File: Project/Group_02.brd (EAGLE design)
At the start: 71.1 x 44.5 mm, 29 parts, among them J1 POWER_JACKPTH_LOCK, U1 +12v

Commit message: Posizionamento holes
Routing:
- net GND: track 10.4 -> 16.1 mm
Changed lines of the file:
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@@
 <setting verticaltext="up"/>
 </settings>
-<grid distance="0.05" unitdist="inch" unit="mm" style="lines" multiple="1" display="yes" altdistance="0.005" altunitdist="inch" altunit="mm"/>
+<grid distance="0.05" unitdist="inch" unit="mil" style="lines" multiple="1" display="yes" altdistance="0.005" altunitdist="inch" altunit="mm"/>
 <layers>
 <layer number="1" name="Top" color="4" fill="1" visible="yes" active="yes"/>
@@
 <dimension x1="-1.27" y1="0" x2="-1.27" y2="44.45" x3="-2.54" y3="22.225" textsize="1.778" layer="51"/>
 <dimension x1="0" y1="46.99" x2="71.12" y2="46.99" x3="35.56" y3="45.72" textsize="1.778" layer="51"/>
+<hole x="3.175" y="42.291" drill="0.9"/>
+<hole x="3.175" y="2.032" drill="0.9"/>
+<hole x="68.58" y="2.032" drill="0.9"/>
+<hole x="68.58" y="42.291" drill="0.9"/>
 </plain>
 <attributes>
@@
 </class>
 </classes>
-<designrules name="default">
+<designrules name="Group_02">
 <description language="de">&lt;b&gt;EAGLE Design Rules&lt;/b&gt;
 &lt;p&gt;
@@
 <param name="mdViaViaSameLayer" value="6mil"/>
 <param name="mnLayersViaInSmd" value="2"/>
-<param name="mdCopperDimension" value="40mil"/>
-<param name="mdDrill" value="6mil"/>
+<param name="mdCopperDimension" value="8mil"/>
+<param name="mdDrill" value="18mil"/>
 <param name="mdSmdStop" value="0mil"/>
-<param name="msWidth" value="6mil"/>
-<param name="msDrill" value="0.35mm"/>
+<param name="msWidth" value="10mil"/>
+<param name="msDrill" value="8mil"/>
 <param name="msMicroVia" value="9.99mm"/>
 <param name="msBlindViaRatio" value="0.5"/>
@@
 <param name="rvMicroViaOuter" value="0.25"/>
 <param name="rvMicroViaInner" value="0.25"/>
-<param name="rlMinPadTop" value="10mil"/>
+<param name="rlMinPadTop" value="8mil"/>
 <param name="rlMaxPadTop" value="20mil"/>
-<param name="rlMinPadInner" value="10mil"/>
+<param name="rlMinPadInner" value="6mil"/>
 <param name="rlMaxPadInner" value="20mil"/>
-<param name="rlMinPadBottom" value="10mil"/>
+<param name="rlMinPadBottom" value="8mil"/>
 <param name="rlMaxPadBottom" value="20mil"/>
-<param name="rlMinViaOuter" value="8mil"/>
+<param name="rlMinViaOuter" value="6mil"/>
 <param name="rlMaxViaOuter" value="20mil"/>
-<param name="rlMinViaInner" value="8mil"/>
+<param name="rlMinViaInner" value="6mil"/>
 <param name="rlMaxViaInner" value="20mil"/>
 <param name="rlMinMicroViaOuter" value="4mil"/>
@@
 <param name="mvStopFrame" value="1"/>
 <param name="mvCreamFrame" value="0"/>
-<param name="mlMinStopFrame" value="4mil"/>
-<param name="mlMaxStopFrame" value="4mil"/>
+<param name="mlMinStopFrame" value="8mil"/>
+<param name="mlMaxStopFrame" value="8mil"/>
 <param name="mlMinCreamFrame" value="0mil"/>
 <param name="mlMaxCreamFrame" value="0mil"/>
@@
 <wire x1="49.149" y1="31.281" x2="50.4834" y2="29.9466" width="0.1524" layer="1"/>
 <wire x1="50.4834" y1="29.9466" x2="52.04596875" y2="29.9466" width="0.1524" layer="1"/>
-<wire x1="20.104" y1="36.395" x2="20.32" y2="36.395" width="0.1524" layer="1"/>
 <via x="21.9506" y="36.9467375" extent="1-16" drill="0.35"/>
 <wire x1="18.704" y1="37.395" x2="18.704" y2="37.811" width="0.1524" layer="1"/>
@@
 <contactref element="U$2" pad="8"/>
 <contactref element="U$2" pad="3"/>
-<polygon width="0.2032" layer="1">
+<polygon width="0.2032" layer="1" isolate="0.3048">
 <vertex x="0" y="0"/>
 <vertex x="0" y="44.45"/>
@@
 <wire x1="34.13896875" y1="37.6936" x2="29.8704" y2="37.6936" width="0.1524" layer="16"/>
 <wire x1="29.8704" y1="37.6936" x2="28.702" y2="38.862" width="0.1524" layer="16"/>
+<wire x1="20.104" y1="36.795" x2="20.139" y2="36.83" width="0.1524" layer="1"/>
+<wire x1="20.139" y1="36.83" x2="21.3438" y2="36.83" width="0.1524" layer="1"/>
+<wire x1="21.3438" y1="36.83" x2="21.3438" y2="37.1980875" width="0.1524" layer="1"/>
+<wire x1="21.3438" y1="37.1980875" x2="21.69925" y2="37.5535375" width="0.1524" layer="1"/>
+<wire x1="21.69925" y1="37.5535375" x2="22.20195" y2="37.5535375" width="0.1524" layer="1"/>
+<wire x1="22.20195" y1="37.5535375" x2="22.5574" y2="37.1980875" width="0.1524" layer="1"/>
+<wire x1="22.5574" y1="37.1980875" x2="22.5574" y2="37.1326" width="0.1524" layer="1"/>
+<wire x1="22.987" y1="36.703" x2="24.892" y2="36.703" width="0.1524" layer="1"/>
+<wire x1="22.5574" y1="37.1326" x2="22.987" y2="36.703" width="0.1524" layer="1"/>
 </signal>
 <signal name="12V">
@@
 <contactref element="R8" pad="1"/>
 <wire x1="31.75" y1="31.75" x2="31.75" y2="33.44" width="0.2032" layer="1"/>
-<wire x1="31.75" y1="33.44" x2="33.02" y2="34.71" width="0.2032" layer="1"/>
+<wire x1="31.75" y1="33.44" x2="32.175" y2="33.865" width="0.2032" layer="1"/>
+<wire x1="32.175" y1="33.865" x2="33.02" y2="34.71" width="0.2032" layer="1"/>
 <wire x1="33.02" y1="34.71" x2="33.417965625" y2="34.312034375" width="0.2032" layer="1"/>
 <wire x1="33.417965625" y1="34.312034375" x2="34.267965625" y2="34.312034375" width="0.2032" layer="1"/>
@@
 <wire x1="13.86659375" y1="35.2298" x2="13.753196875" y2="35.343196875" width="0.2032" layer="1"/>
 <wire x1="13.753196875" y1="35.343196875" x2="13.626196875" y2="35.343196875" width="0.2032" layer="1"/>
-<wire x1="13.626196875" y1="35.343196875" x2="10.16" y2="31.877" width="0.2032" layer="1"/>
-<wire x1="16.075" y1="36.395" x2="14.9098" y2="35.2298" width="0.2032" layer="1"/>
+<wire x1="13.626196875" y1="35.343196875" x2="10.16" y2="31.877" width="0.254" layer="1"/>
+<wire x1="16.075" y1="36.395" x2="14.9098" y2="35.2298" width="0.254" layer="1"/>
 <wire x1="14.9098" y1="35.2298" x2="13.86659375" y2="35.2298" width="0.2032" layer="1"/>
 </signal>
@@
 <wire x1="12.7" y1="31.623" x2="12.7" y2="33.02" width="0.2032" layer="1"/>
 <wire x1="14.5542" y1="34.8742" x2="15.0571" y2="34.8742" width="0.2032" layer="1"/>
-<wire x1="16.1779" y1="35.995" x2="18.504" y2="35.995" width="0.2032" layer="1"/>
+<wire x1="16.1779" y1="35.995" x2="18.504" y2="35.995" width="0.254" layer="1"/>
 <wire x1="15.0571" y1="34.8742" x2="16.1779" y2="35.995" width="0.2032" layer="1"/>
 <wire x1="12.7" y1="33.02" x2="14.5542" y2="34.8742" width="0.2032" layer="1"/>

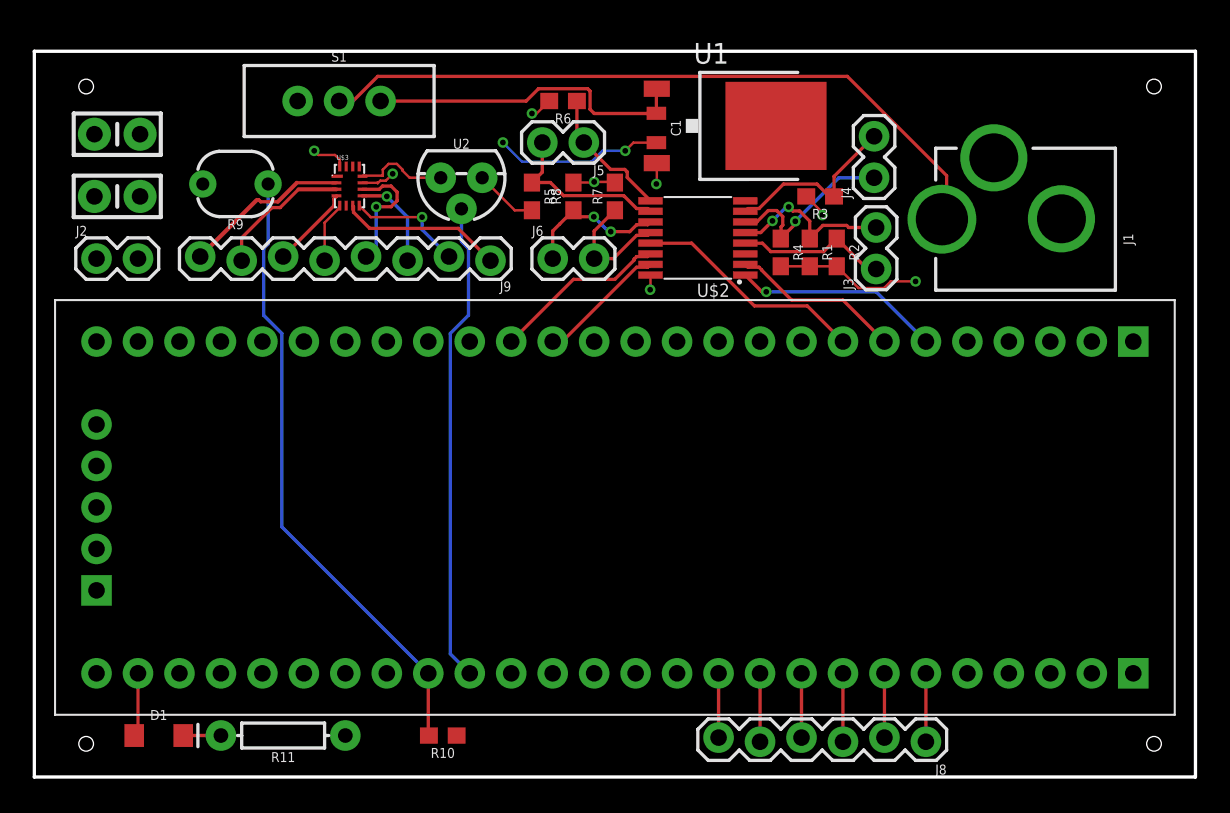
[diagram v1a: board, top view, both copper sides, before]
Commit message: Aggiornamento M3 holes
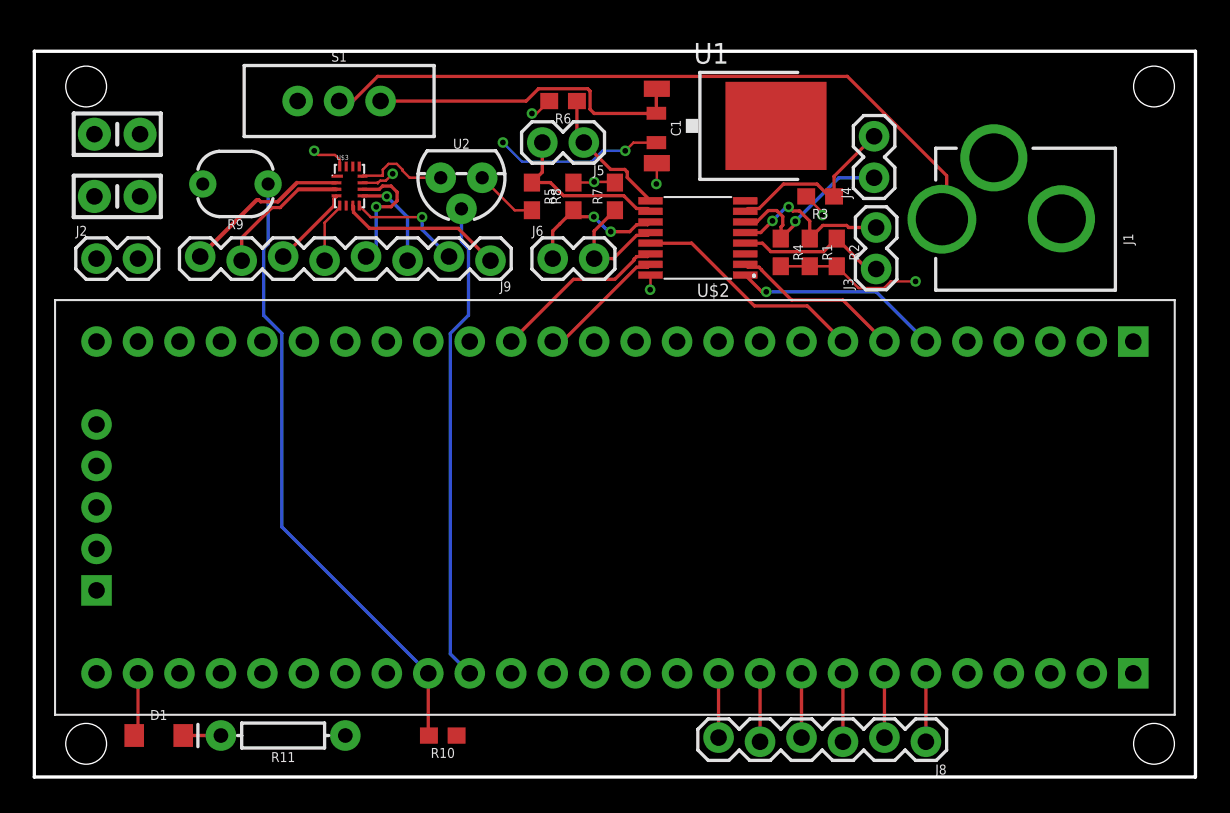
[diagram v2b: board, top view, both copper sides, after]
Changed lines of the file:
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@@
 <setting verticaltext="up"/>
 </settings>
-<grid distance="0.05" unitdist="inch" unit="mil" style="lines" multiple="1" display="yes" altdistance="0.005" altunitdist="inch" altunit="mm"/>
+<grid distance="0.05" unitdist="inch" unit="mm" style="lines" multiple="1" display="yes" altdistance="0.005" altunitdist="inch" altunit="mm"/>
 <layers>
 <layer number="1" name="Top" color="4" fill="1" visible="yes" active="yes"/>
@@
 <dimension x1="-1.27" y1="0" x2="-1.27" y2="44.45" x3="-2.54" y3="22.225" textsize="1.778" layer="51"/>
 <dimension x1="0" y1="46.99" x2="71.12" y2="46.99" x3="35.56" y3="45.72" textsize="1.778" layer="51"/>
-<hole x="3.175" y="42.291" drill="0.9"/>
-<hole x="3.175" y="2.032" drill="0.9"/>
-<hole x="68.58" y="2.032" drill="0.9"/>
-<hole x="68.58" y="42.291" drill="0.9"/>
+<hole x="3.175" y="42.291" drill="2.5"/>
+<hole x="3.175" y="2.032" drill="2.5"/>
+<hole x="68.58" y="2.032" drill="2.5"/>
+<hole x="68.58" y="42.291" drill="2.5"/>
 </plain>
 <attributes>
@@
 <via x="17.145" y="38.354" extent="1-16" drill="0.35"/>
 <wire x1="18.415" y1="38.1" x2="17.399" y2="38.1" width="0.1524" layer="1"/>
+<wire x1="47.498" y1="31.281" x2="48.26" y2="34.4172" width="0" layer="19" extent="1-1"/>
+<wire x1="37.74" y1="30.745" x2="45.72" y2="31.281" width="0" layer="19" extent="1-1"/>
+<wire x1="38.1" y1="36.322" x2="37.74" y2="30.745" width="0" layer="19" extent="1-1"/>
+<wire x1="35.56" y1="36.41" x2="38.1" y2="36.322" width="0" layer="19" extent="1-1"/>
+<wire x1="30.48" y1="34.71" x2="33.02" y2="36.41" width="0" layer="19" extent="1-1"/>
+<wire x1="30.48" y1="40.64" x2="33.02" y2="36.41" width="0" layer="19" extent="1-1"/>
+<wire x1="21.9506" y1="36.9467375" x2="27.432" y2="36.703" width="0" layer="19" extent="1-1"/>
+<wire x1="18.704" y1="37.395" x2="20.104" y2="36.395" width="0" layer="19" extent="1-1"/>
+<wire x1="10.319" y1="36.322" x2="17.145" y2="38.354" width="0" layer="19" extent="1-1"/>
+<wire x1="6.477" y1="35.56" x2="10.319" y2="36.322" width="0" layer="19" extent="1-1"/>
+<wire x1="6.477" y1="39.37" x2="6.477" y2="35.56" width="0" layer="19" extent="1-1"/>
+<wire x1="6.35" y1="31.75" x2="6.477" y2="35.56" width="0" layer="19" extent="1-1"/>
+<wire x1="3.81" y1="26.67" x2="6.35" y2="31.75" width="0" layer="19" extent="1-1"/>
+<wire x1="67.31" y1="6.35" x2="53.975" y2="30.353" width="0" layer="19" extent="1-1"/>
 </signal>
 <signal name="GND">
@@
 <wire x1="22.987" y1="36.703" x2="24.892" y2="36.703" width="0.1524" layer="1"/>
 <wire x1="22.5574" y1="37.1326" x2="22.987" y2="36.703" width="0.1524" layer="1"/>
+<wire x1="62.912" y1="34.1884" x2="58.769" y2="37.9246" width="0" layer="19" extent="1-1"/>
+<wire x1="45.426" y1="39.878" x2="58.769" y2="37.9246" width="0" layer="19" extent="1-1"/>
+<wire x1="43.54" y1="35.295" x2="45.426" y2="39.878" width="0" layer="19" extent="1-1"/>
+<wire x1="43.54" y1="32.045" x2="43.54" y2="35.295" width="0" layer="19" extent="1-1"/>
+<wire x1="38.1" y1="38.851" x2="43.54" y2="35.295" width="0" layer="19" extent="1-1"/>
+<wire x1="24.892" y1="36.703" x2="28.702" y2="38.862" width="0" layer="19" extent="1-1"/>
+<wire x1="3.683" y1="35.56" x2="20.104" y2="36.795" width="0" layer="19" extent="1-1"/>
+<wire x1="3.683" y1="39.37" x2="3.683" y2="35.56" width="0" layer="19" extent="1-1"/>
+<wire x1="3.81" y1="31.75" x2="3.683" y2="35.56" width="0" layer="19" extent="1-1"/>
+<wire x1="6.35" y1="26.67" x2="3.81" y2="31.75" width="0" layer="19" extent="1-1"/>
+<wire x1="19.05" y1="2.54" x2="6.35" y2="26.67" width="0" layer="19" extent="1-1"/>
+<wire x1="25.869" y1="2.54" x2="19.05" y2="2.54" width="0" layer="19" extent="1-1"/>
+<wire x1="64.77" y1="6.35" x2="62.912" y2="34.1884" width="0" layer="19" extent="1-1"/>
 </signal>
 <signal name="12V">

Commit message: Routing width 10 mils
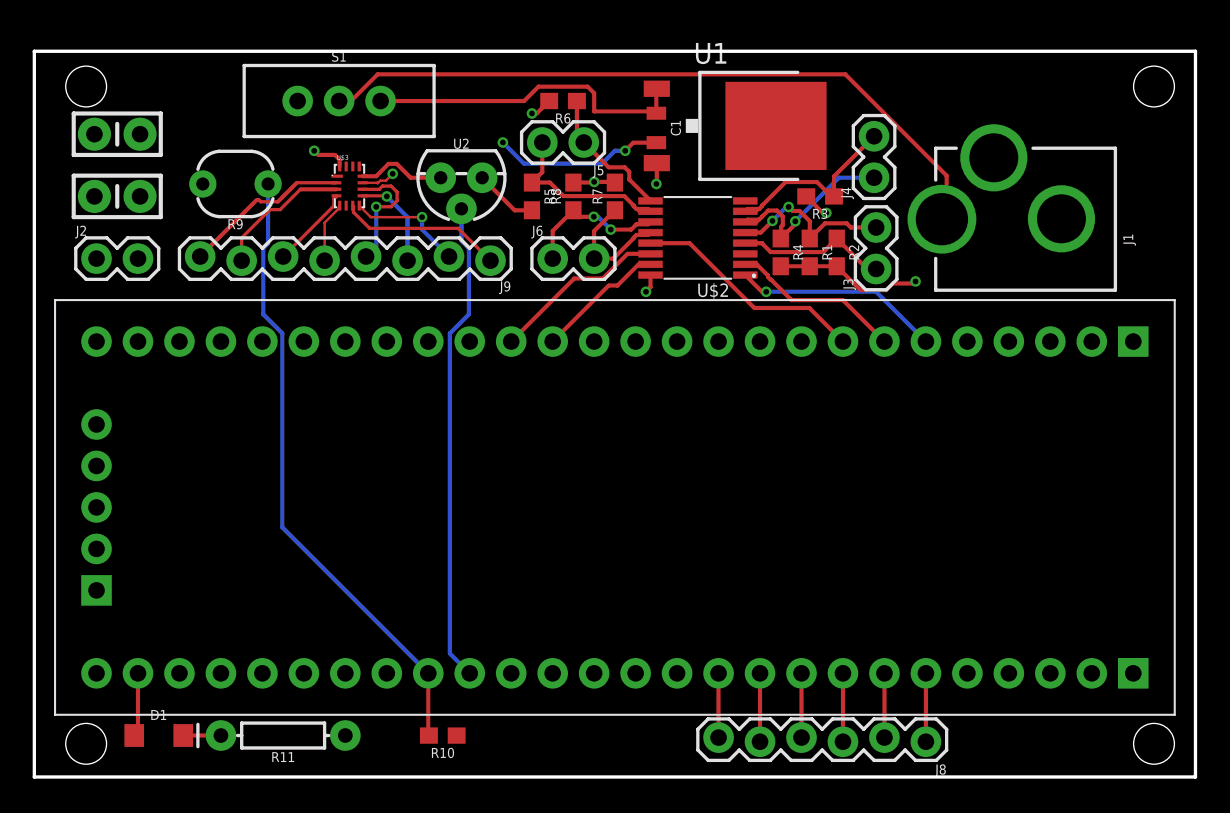
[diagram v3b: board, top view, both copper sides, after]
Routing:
- net I2C_SCL_1: track 11.1 -> 12.0 mm
- net I2C_A1: track 10.5 -> 11.3 mm
- net I2C_SCL_2: track 10.7 -> 11.5 mm
- net I2C_SDA_1: track 11.5 -> 12.2 mm
